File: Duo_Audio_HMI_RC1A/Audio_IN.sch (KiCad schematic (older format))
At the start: 128 parts, among them J1 JACK_P10_TRS_6P, J2 JACK_P10_TRS_6P

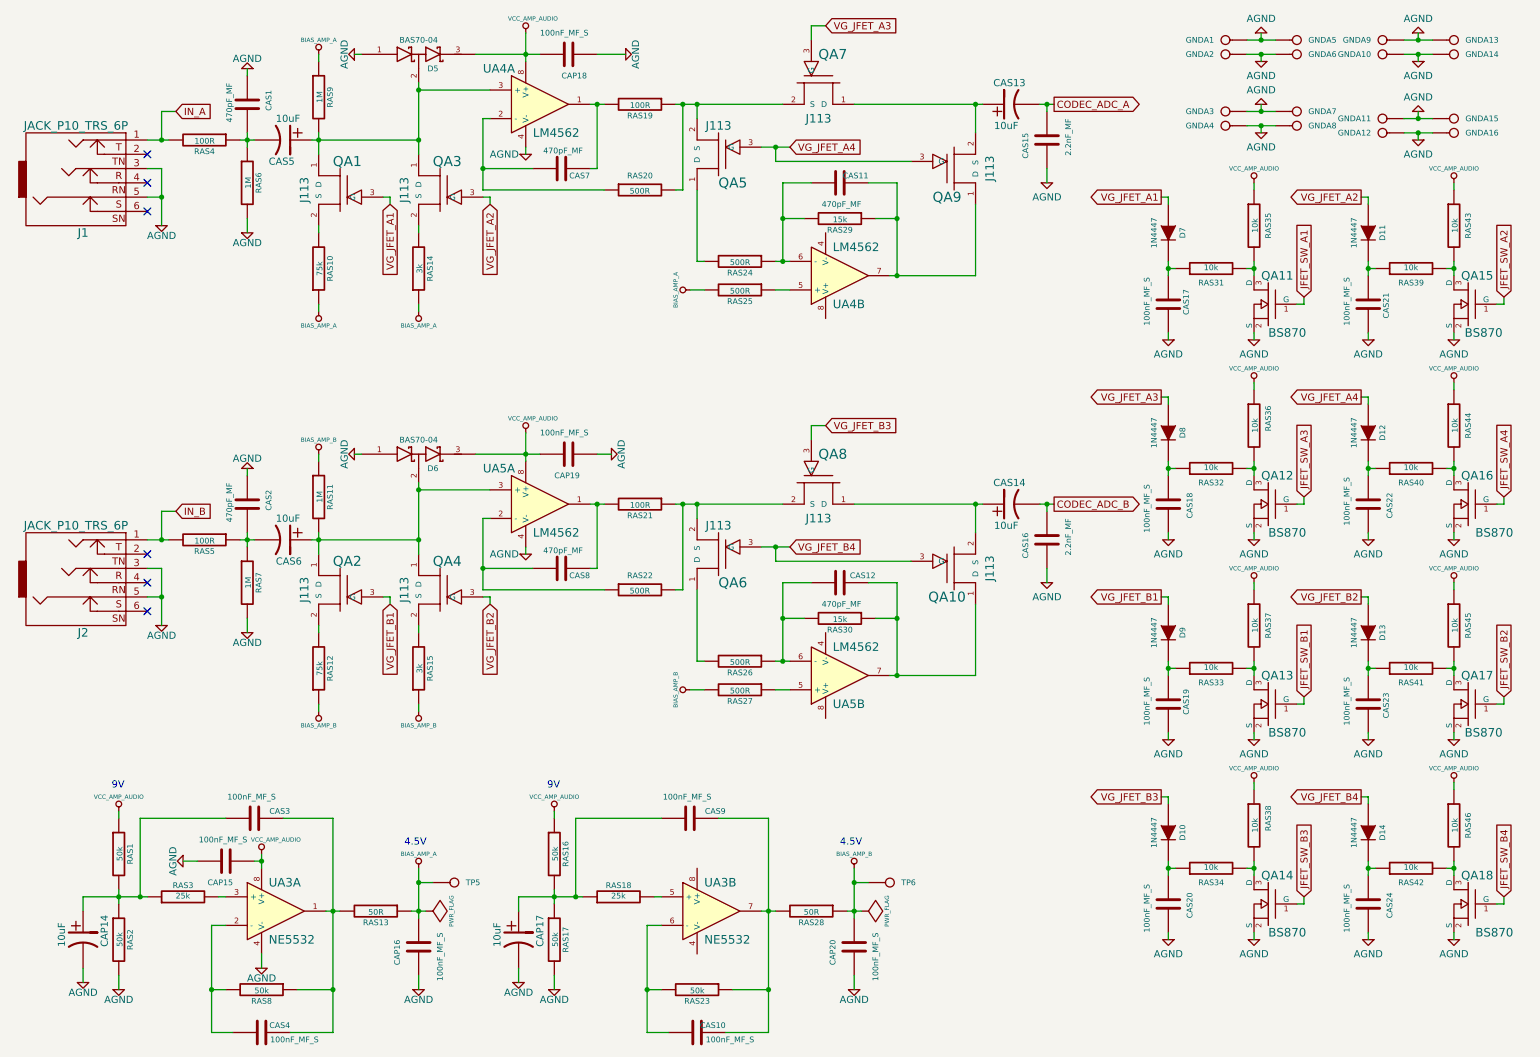
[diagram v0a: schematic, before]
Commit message: Finished RCA1 schematic of the Baseboard and the Pannelboard with USB OTG. Board dimensions, most footprint attribution and major placement implemented in layout. Learning GIT!
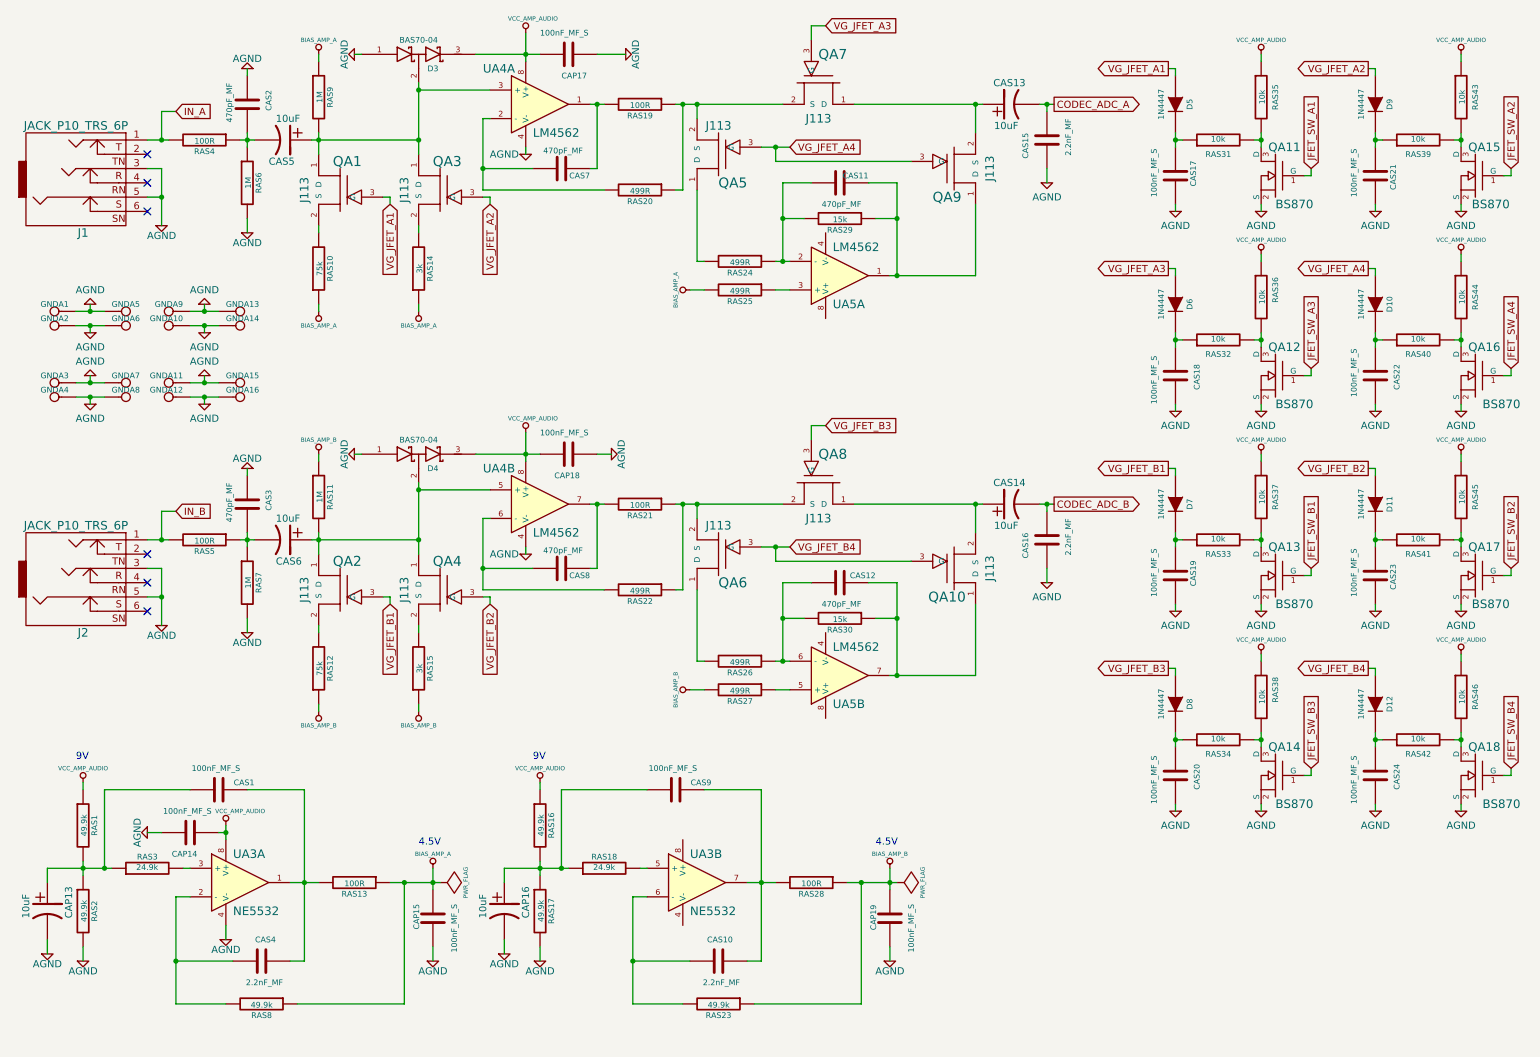
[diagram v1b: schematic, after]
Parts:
- removed TP5, TP6: CONN_1, SIL-1, symbol CONN_1
- CAS10, CAS4: value 100nF_MF_S -> 2.2nF_MF
- GNDA1, GNDA10, GNDA11, GNDA12, GNDA13, GNDA14, GNDA15, GNDA16, GNDA2, GNDA3, GNDA4, GNDA5, GNDA6, GNDA7, GNDA8, GNDA9: value CONN_1 -> PAD_GND
- RAS1, RAS16, RAS17, RAS2, RAS23, RAS8: value 50k -> 49.9k
- RAS13, RAS28: value 50R -> 100R
- RAS18, RAS3: value 25k -> 24.9k
- RAS20, RAS22, RAS24, RAS25, RAS26, RAS27: value 500R -> 499R
- renumbered CAP14 to CAP13, CAP15 to CAP14, CAP16 to CAP15, CAP17 to CAP16, CAP18 to CAP17, CAP19 to CAP18, CAP20 to CAP19, CAS3 to CAS1, CAS1 to CAS2, CAS2 to CAS3, D12 to D10, D13 to D11, D14 to D12, D5 to D3, D6 to D4, D7 to D5, D8 to D6, D9 to D7, D10 to D8, D11 to D9, UA5 to UA4, UA4 to UA5
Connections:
- net BIAS_AMP_A: now also RAS8.1
- net BIAS_AMP_B: now also RAS23.1
- net at CAS1.2, CAS4.2, RAS13.2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: no longer RAS8.1
- net at CAS10.2, CAS9.2, RAS28.2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: no longer RAS23.1
- net at CAS7.1, UA4.2 (-): now also RAS20.2; no longer RAS20.1
- net at QA5.2 (S), QA7.2 (S), RAS19.1: now also RAS20.1; no longer RAS20.2
- net at RAS25.1: now also UA5.3 (+); no longer UA5.5 (+)
- net at CAS11.1, RAS24.1, RAS29.2: now also UA5.2 (-); no longer UA5.6 (-)
- net at CAS11.2, QA9.1 (D), RAS29.1: now also UA5.1; no longer UA5.7
- net at CAS8.2, RAS21.2: now also UA4.7; no longer UA4.1
- net at CAS6.1, D4.2 (AK), QA2.1 (D)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: now also UA4.5 (+); no longer UA4.3 (+)
- net at QA6.2 (S), QA8.2 (S), RAS21.1: now also RAS22.1; no longer RAS22.2
- new net: CAS8.1, RAS22.2, UA4.6 (-)
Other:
- moved on the sheet: CAP13, CAP14, CAP15, CAP16, CAP19, CAS1, CAS10, CAS17, CAS18, CAS19, CAS20, CAS21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
